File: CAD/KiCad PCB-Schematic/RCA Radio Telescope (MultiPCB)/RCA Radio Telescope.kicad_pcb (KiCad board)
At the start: 2 copper layers, 298.5 x 183.4 mm, 72 parts, among them J1 5V In For Filter Board, J10 FILTER_OUT, J11 ANT, J11 Screw_Terminal_01x04, J13 Screw_Terminal_01x04, J15 ANT, J2 9-12V From PoE Splitter, J3 3V Out For LNA, J4 5V Out For Filter Board, J5 Input from SDR, J7 USB_A, J8 USB_A, J9 ANT, Q1 DMP4047LFDE-7, U13 MAX8510EXK30T, U14 TPS62133RGTR, U15 BPF-A1340+, U3 SKY13588-460LF, U4 SKY13588-460LF, U5 SN74AVC2T45DCUR, U6 MIC5365-1.8YC5-TR, U7 MIC5365-3.3YC5-TR

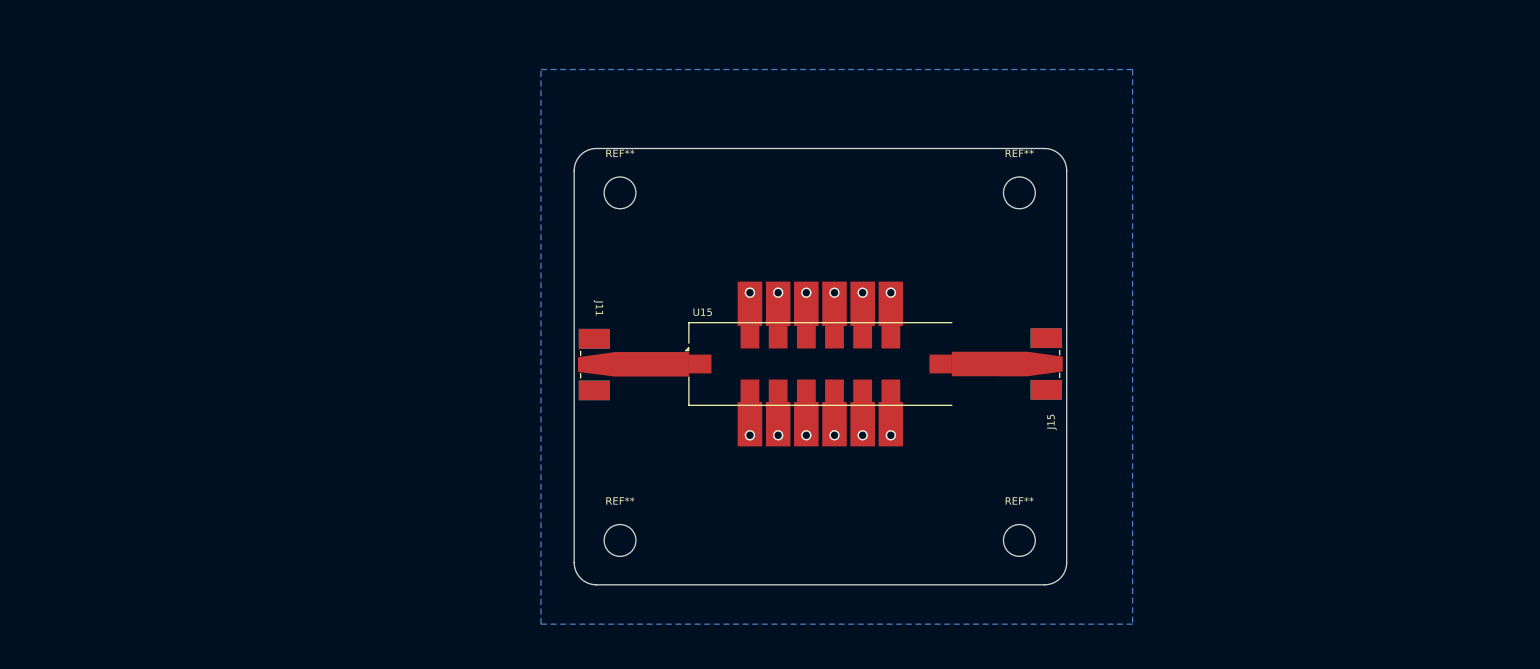
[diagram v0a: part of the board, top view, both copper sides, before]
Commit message: Add 1.6 GHZ Matching Network PCB v1.0
- Same design as original board, but with 1.6 GHz matching network
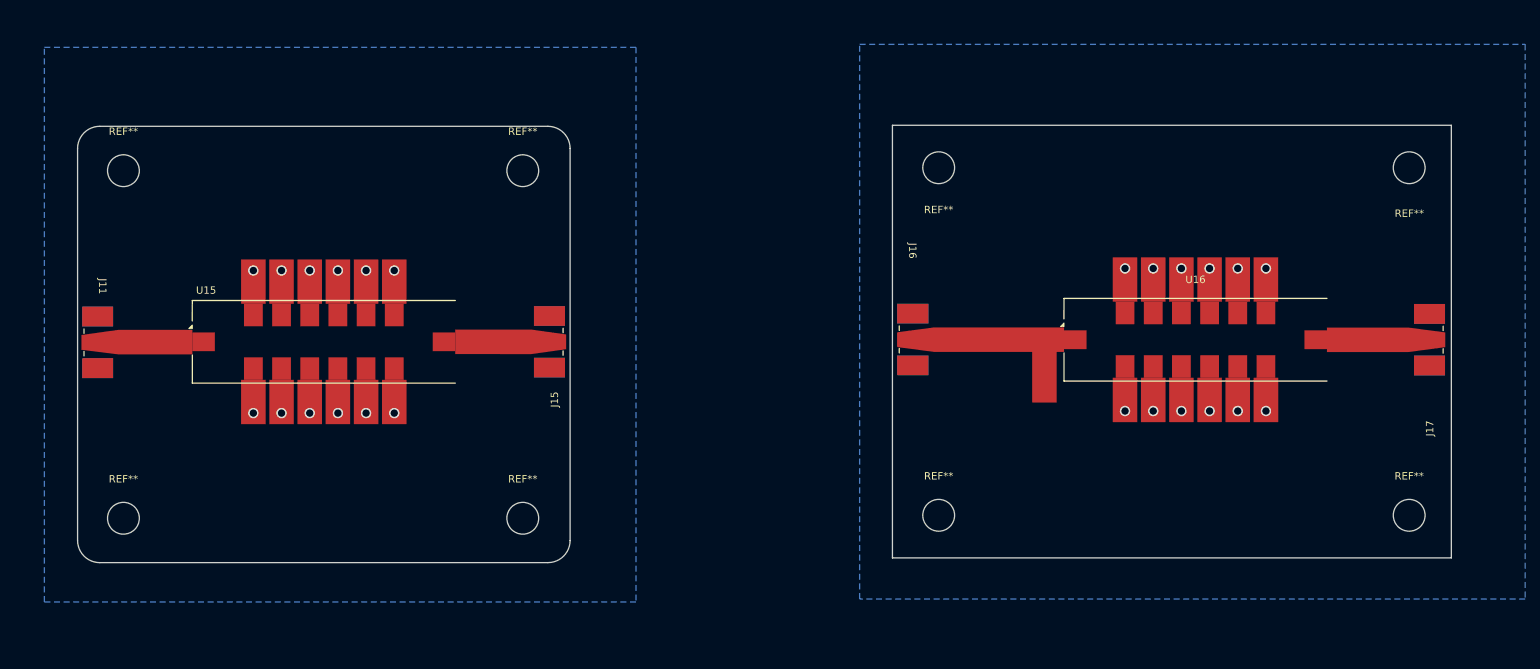
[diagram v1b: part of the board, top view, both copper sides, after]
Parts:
- added J16: ANT, Library:CONN_142-0711-821_CIN, F.Cu at (310.6, 71.8)
- added J17: ANT, Library:CONN_142-0711-821_CIN, F.Cu at (370.5, 71.9)
- added REF**: MountingHole_4.3mm_M4, MountingHole:MountingHole_4.3mm_M4, F.Cu at (372.7, 95.6)
- added REF**: MountingHole_4.3mm_M4, MountingHole:MountingHole_4.3mm_M4, F.Cu at (309.1, 95.6)
- added REF**: MountingHole_4.3mm_M4, MountingHole:MountingHole_4.3mm_M4, F.Cu at (309.1, 48.6)
- added REF**: MountingHole_4.3mm_M4, MountingHole:MountingHole_4.3mm_M4, F.Cu at (372.7, 48.6)
- added SIXSF: Kikit_Board_Label, Library:Kikit_Board_Label, F.Cu at (319.1, 42.6)
- added U16: BPF-A1340+, RF_Mini-Circuits:Mini-Circuits_HQ1157, F.Cu at (343.8, 71.9)
- moved J11 67.2 mm to (200.3, 72.2)
- moved J15 67.2 mm to (251.5, 72.1)
- moved REF** 67.2 mm to (252.8, 96.0)
- moved REF** 67.2 mm to (198.8, 49.0)
- moved REF** 67.2 mm to (198.8, 96.0)
- moved REF** 67.2 mm to (252.8, 49.0)
- moved SF 67.2 mm to (208.8, 43.0)
- moved U15 67.2 mm to (225.9, 72.1)
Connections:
- J11 pad 4: /SMDFilter/GND -> (no net)
- J11 pad 6: /SMDFilter/GND -> (no net)
- J15 pad 4: /SMDFilter/GND -> (no net)
- J15 pad 6: /SMDFilter/GND -> (no net)
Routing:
- net /1-6GHz-SMDFilter/GND: vias 0 -> 12
- added copper zone on B.Cu, net /1-6GHz-SMDFilter/GND
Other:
- board size 298.5 x 183.4 mm -> 350.5 x 183.4 mm
- board text added: "1.6GHz Matching Network SMD Filter PCB Rev v1.0 4/25/2025"

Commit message: Added Coupled Lines Filter PCB v1.0 and Exported PD Board Step File
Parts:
- added J18: ANT, Library:CONN_142-0711-821_CIN, F.Cu at (458.9, 42.5)
- added J19: ANT, Library:CONN_142-0711-821_CIN, F.Cu at (605.7, 48.5)
- added SIXSF: Kikit_Board_Label, Library:Kikit_Board_Label, F.Cu at (467.8, 28.3)
- moved J10 59.5 mm to (89.2, 222.8)
- moved MN 59.5 mm to (98.7, 173.8)
- moved C13 59.5 mm to (131.7, 201.8)
- moved C14 59.5 mm to (131.8, 243.8)
- moved C15 59.5 mm to (131.7, 223.8)
- moved J13 59.5 mm to (112.9, 176.8)
- moved J9 59.5 mm to (183.7, 222.8)
- moved L1 59.5 mm to (142.7, 202.8)
- moved L3 59.5 mm to (142.7, 242.8)
- moved L4 59.5 mm to (142.7, 222.8)
- moved U3 59.5 mm to (156.1, 222.8)
- moved U4 59.5 mm to (116.7, 222.8)
- moved J11 13.0 mm to (212.8, 68.7)
- moved J15 13.0 mm to (264.0, 68.7)
- moved J16 13.0 mm to (323.1, 68.3)
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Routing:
- added copper zone on B.Cu, net /Coupled Lines Filter/GND
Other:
- board size 350.5 x 183.4 mm -> 585.8 x 231 mm
- board text added: "Coupled Lines SMD Filter PCB Rev v1.0 4/25/2025"

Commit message: RF Boards Redo (WIP)
- Overhauling current RF boards to keep 4 RF boards in total
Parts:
- removed C13, C14, C15: C, Capacitor_SMD:C_0805_2012Metric
- removed J13: Screw_Terminal_01x04, Connector_PinHeader_2.54mm:PinHeader_1x04_P2.54mm_Vertical
- removed L1, L3, L4: L, Inductor_SMD:L_0805_2012Metric
- removed MN, SIXSF (x2): Kikit_Board_Label, Library:Kikit_Board_Label
- removed the REF** at (385.2, 92.1)
- removed the REF** at (321.6, 92.1)
- removed the REF** at (321.6, 45.1)
- removed the REF** at (385.2, 45.1)
- added C1: 1 uF, Capacitor_SMD:C_0805_2012Metric, F.Cu at (97.0, 183.0)
- added C2: 1 uF, Capacitor_SMD:C_0805_2012Metric, F.Cu at (101.0, 183.1)
- added C3: 1 uF, Capacitor_SMD:C_0805_2012Metric, F.Cu at (108.0, 183.1)
- added C4: 1 uF, Capacitor_SMD:C_0805_2012Metric, F.Cu at (111.0, 183.1)
- added J1: Screw_Terminal_01x04, Library:PHOENIX_1729144, F.Cu at (75.1, 184.6)
- added J11: ANT, Library:CONN_142-0711-821_CIN, F.Cu at (162.5, 118.5)
- added J15: ANT, Library:CONN_142-0711-821_CIN, F.Cu at (162.5, 128.6)
- added TP12: FCTRL_VIN, Library:TestPoint_Pad_D1.0mm_Edit, F.Cu at (108.0, 205.0)
- added TP13: FCTRL_1V8, Library:TestPoint_Pad_D1.0mm_Edit, F.Cu at (108.0, 208.1)
- added TP14: FCTRL_3V3, Library:TestPoint_Pad_D1.0mm_Edit, F.Cu at (108.0, 211.1)
- added TP15: FCTRL_GND, Library:TestPoint_Pad_1.5x1.5mm_Edit, F.Cu at (69.9, 226.5)
- added U5: SN74AVC2T45DCUR, Library:DCU8, F.Cu at (99.0, 177.0)
- added U6: MIC5365-1.8YC5-TR, Library:SOT65P210X110-5N, F.Cu at (92.0, 183.0)
- added U7: MIC5365-3.3YC5-TR, Library:SOT65P210X110-5N, F.Cu at (82.0, 216.0)
- moved J19 449.6 mm to (273.7, 351.7)
- moved J16 426.3 mm to (8.38, 356.0)
- moved J18 418.0 mm to (177.6, 351.7)
- moved J17 399.7 mm to (104.4, 355.0)
- moved U16 397.2 mm to (81.7, 355.4)
- moved J9 153.5 mm to (31.0, 206.8), turned to 0 degrees
- moved U3 94.6 mm to (61.7, 227.0), turned to 0 degrees
- moved U4 51.0 mm to (66.0, 227.0), turned to 0 degrees
- moved J10 28.3 mm to (68.0, 204.0), turned to 0 degrees
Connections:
- net /1-6GHz-SMDFilter/GND renamed /Matched SMD Filter/GND
- net /1-6GHz-SMDFilter/SIGNAL_IN renamed /Matched SMD Filter/SIGNAL_IN
- net /1-6GHz-SMDFilter/SIGNAL_OUT renamed /Matched SMD Filter/SIGNAL_OUT
- net /MatchNetwork/+3V3 renamed /RFSwitchFilter/+3V3
- net /MatchNetwork/ANT renamed /RFSwitchFilter/ANT
- net /MatchNetwork/FILTER_OUT renamed /RFSwitchFilter/FILTER_OUT
- net /MatchNetwork/INT_CTRL_V1 renamed /RFSwitchFilter/INT_CTRL_V1
- net /MatchNetwork/INT_CTRL_V2 renamed /RFSwitchFilter/INT_CTRL_V2
- J18 pad 1: /Coupled Lines Filter/SIGNAL_IN -> /Matched Distributive Filter/SIGNAL_IN
- J18 pad 4: /Coupled Lines Filter/GND -> (no net)
- J18 pad 6: /Coupled Lines Filter/GND -> (no net)
- J19 pad 1: /Coupled Lines Filter/SIGNAL_OUT -> /Matched Distributive Filter/SIGNAL_IN
- U3 pad 1: /MatchNetwork/FILTERA_IN -> /RFSwitchFilter/FILTERA_IN
- U3 pad 3: /MatchNetwork/FILTERC_IN -> /RFSwitchFilter/FILTERC_IN
- U3 pad 9: /MatchNetwork/FILTERB_IN -> /RFSwitchFilter/FILTERB_IN
- U4 pad 1: /MatchNetwork/FILTERB_OUT -> /RFSwitchFilter/FILTERB_IN
- U4 pad 3: /MatchNetwork/FILTERC_OUT -> /RFSwitchFilter/FILTERC_IN
- U4 pad 9: /MatchNetwork/FILTERA_OUT -> /RFSwitchFilter/FILTERA_IN
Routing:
- net /RFSwitchFilter/INT_CTRL_V2: track 152.7 -> 0.00 mm, vias 2 -> 0
- net /RFSwitchFilter/+3V3: track 150.0 -> 0.00 mm, vias 3 -> 0
- net /RFSwitchFilter/INT_CTRL_V1: track 144.7 -> 0.00 mm, vias 3 -> 0
- net /MatchNetwork/FILTERA_OUT: track 39.0 -> 0.00 mm
- net /MatchNetwork/FILTERB_OUT: track 37.8 -> 0.00 mm
- net /MatchNetwork/FILTERC_OUT: track 27.5 -> 0.00 mm
- net /MatchNetwork/FILTERA_IN: track 26.2 -> 0.00 mm
- net /MatchNetwork/FILTERB_IN: track 25.0 -> 0.00 mm
- net /RFSwitchFilter/FILTER_OUT: track 19.2 -> 0.00 mm
- net /RFSwitchFilter/ANT: track 19.2 -> 0.00 mm
- net /MatchNetwork/FILTERC_IN: track 14.3 -> 0.00 mm
- net (no net): track 0.00 -> 5.24 mm
- net /Matched SMD Filter/GND: vias 12 -> 0
- net /MN_GND: vias 156 -> 0
- removed copper zone on B.Cu, net /Coupled Lines Filter/GND
- removed copper zone on B.Cu, net /MN_GND
- removed copper zone on F.Cu, net /MN_GND
- removed copper zone on B.Cu, net /Matched SMD Filter/GND
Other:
- board size 585.8 x 231 mm -> 243.8 x 78.8 mm
- board text added: "Matched Distributive Filter PCB Rev v1.3 4/11/2025"
- board text added: "Matched SMD Filter PCB Rev v1.0 4/29/2025"
- board text removed: "1.6GHz Matching Network SMD Filter PCB Rev v1.0 4/25/2025"
- board text removed: "Coupled Lines SMD Filter PCB Rev v1.0 4/25/2025"
- board text removed: "Matching Network PCB Rev v1.0 4/3/2025"

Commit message: Added 4 RF Board Designs into KiCAD project
- Added Matched SMD Filter Board, Matched Distributive Filter Board, RF Switch Filter Board, and kept original SMD Filter Board
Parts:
- removed the C1 at (151.0, 33.0)
- removed the C2 at (151.0, 38.5)
- removed the C3 at (143.1, 33.9)
- removed the C4 at (145.2, 37.4)
- removed FC: Kikit_Board_Label, Library:Kikit_Board_Label
- removed the J1 at (156.6, 34.5)
- removed the J11 at (162.5, 118.5)
- removed the J11 at (141.0, 41.0)
- removed the J15 at (162.5, 128.6)
- removed the REF** at (265.3, 92.5)
- removed the REF** at (211.3, 45.5)
- removed the REF** at (211.3, 92.5)
- removed the REF** at (265.3, 45.5)
- removed the TP12 at (153.6, 29.2)
- removed the TP13 at (145.1, 34.5)
- removed the TP14 at (143.1, 36.7)
- removed TP15 (x2): FCTRL_GND, Library:TestPoint_Pad_1.5x1.5mm_Edit
- removed the U5 at (140.6, 34.6)
- removed the U6 at (148.1, 33.2)
- removed the U7 at (148.0, 37.6)
- added MDF: Kikit_Board_Label, Library:Kikit_Board_Label, F.Cu at (40.9, 222.2)
- added MSF: Kikit_Board_Label, Library:Kikit_Board_Label, F.Cu at (40.5, 136.1)
- added REF**: MountingHole_4.3mm_M4, MountingHole:MountingHole_4.3mm_M4, F.Cu at (135.0, 256.0)
- added REF**: MountingHole_4.3mm_M4, MountingHole:MountingHole_4.3mm_M4, F.Cu at (186.0, 65.0)
- added REF**: MountingHole_4.3mm_M4, MountingHole:MountingHole_4.3mm_M4, F.Cu at (186.0, 110.0)
- added REF**: MountingHole_4.3mm_M4, MountingHole:MountingHole_4.3mm_M4, F.Cu at (35.0, 256.0)
- added REF**: MountingHole_4.3mm_M4, MountingHole:MountingHole_4.3mm_M4, F.Cu at (36.0, 142.0)
- added REF**: MountingHole_4.3mm_M4, MountingHole:MountingHole_4.3mm_M4, F.Cu at (257.0, 175.0)
- added REF**: MountingHole_4.3mm_M4, MountingHole:MountingHole_4.3mm_M4, F.Cu at (143.0, 142.0)
- added REF**: MountingHole_4.3mm_M4, MountingHole:MountingHole_4.3mm_M4, F.Cu at (307.0, 110.0)
- added REF**: MountingHole_4.3mm_M4, MountingHole:MountingHole_4.3mm_M4, F.Cu at (307.0, 65.0)
- added REF**: MountingHole_4.3mm_M4, MountingHole:MountingHole_4.3mm_M4, F.Cu at (36.0, 171.0)
- added REF**: MountingHole_4.3mm_M4, MountingHole:MountingHole_4.3mm_M4, F.Cu at (135.0, 229.0)
- added REF**: MountingHole_4.3mm_M4, MountingHole:MountingHole_4.3mm_M4, F.Cu at (202.0, 175.0)
- added REF**: MountingHole_4.3mm_M4, MountingHole:MountingHole_4.3mm_M4, F.Cu at (202.0, 222.0)
- added REF**: MountingHole_4.3mm_M4, MountingHole:MountingHole_4.3mm_M4, F.Cu at (143.0, 171.0)
- added REF**: MountingHole_4.3mm_M4, MountingHole:MountingHole_4.3mm_M4, F.Cu at (35.0, 229.0)
- added REF**: MountingHole_4.3mm_M4, MountingHole:MountingHole_4.3mm_M4, F.Cu at (257.0, 222.0)
- added RFS: Kikit_Board_Label, Library:Kikit_Board_Label, F.Cu at (194.3, 59.0)
- added U17: BPF-A355, RF_Mini-Circuits:Mini-Circuits_HQ1157, F.Cu at (279.0, 95.9)
- C1, C2, C3, C4, TP12, TP13, TP14, U6, U7: moved to B.Cu
- J5: value Input from SDR -> 5V From SDR; footprint Library:PHOENIX_1729144 -> Library:CONN_1729128_PXC
- U5: value SN74AVC2T45DCUR -> SN74AVC2T244DQER; footprint Library:DCU8 -> Library:SON35P140X100X40-8N; moved to B.Cu
- moved J10 260.4 mm to (304.8, 95.8), turned to 90 degrees
- moved U4 231.8 mm to (257.1, 95.9), turned to -90 degrees
- moved U7 213.7 mm to (242.0, 74.4), turned to -90 degrees
- moved U16 202.4 mm to (114.6, 155.6)
- moved J17 202.4 mm to (140.6, 155.9)
- moved J16 202.2 mm to (38.1, 156.0)
- moved J1 197.5 mm to (228.3, 60.0), turned to 180 degrees
- moved TP12 191.0 mm to (244.5, 71.4), turned to 180 degrees
- moved J9 190.9 mm to (187.4, 97.4), turned to -90 degrees
- moved U3 190.3 mm to (201.1, 97.4), turned to 90 degrees
- moved TP14 188.6 mm to (239.0, 75.4), turned to 180 degrees
- moved TP13 180.9 mm to (231.0, 75.4), turned to 180 degrees
- moved U6 178.6 mm to (233.7, 74.4), turned to -90 degrees
- moved J18 178.3 mm to (36.8, 242.3)
- moved J19 178.1 mm to (133.1, 242.3)
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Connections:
- C1 pad 2: /MN_GND -> /RFS_GND
- C2 pad 2: /MN_GND -> /RFS_GND
- C3 pad 1: /MN_GND -> /RFS_GND
- C4 pad 1: /MN_GND -> /RFS_GND
- J1 pad 1: /MN_GND -> /RFS_GND
- J18 pad 1: /Matched Distributive Filter/SIGNAL_IN -> /Matched Distributive Filter/GND
- J19 pad 1: /Matched Distributive Filter/SIGNAL_IN -> /Matched Distributive Filter/GND
- J5 pad 1: /SDR_GPO_VDD -> /RFSwitchFilter/5V_IN
- J5 pad 2: /SDR_GPO_0 -> /RFS_GND
- U3 pad 10: /MN_GND -> /RFS_GND
- U3 pad 12: /MN_GND -> /RFS_GND
- U3 pad 13: /MN_GND -> /RFS_GND
- U3 pad 2: /MN_GND -> /RFS_GND
- U3 pad 7: /MN_GND -> /RFS_GND
- U3 pad 8: /MN_GND -> /RFS_GND
- U4 pad 10: /MN_GND -> /RFS_GND
- U4 pad 11: /RFSwitchFilter/FILTER_OUT -> Net-(U17-IN)
- U4 pad 12: /MN_GND -> /RFS_GND
- U4 pad 13: /MN_GND -> /RFS_GND
- U4 pad 2: /MN_GND -> /RFS_GND
- U4 pad 7: /MN_GND -> /RFS_GND
- U4 pad 8: /MN_GND -> /RFS_GND
- U5 pad 4: /MN_GND -> /RFSwitchFilter/VDD_REF
- U5 pad 5: /RFSwitchFilter/VDD_REF -> /RFS_GND
- U6 pad 2: /MN_GND -> /RFS_GND
- U7 pad 2: /MN_GND -> /RFS_GND
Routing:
- net /RFSwitchFilter/INT_CTRL_V1: track 0.00 -> 120.4 mm, vias 0 -> 4
- net /RFSwitchFilter/INT_CTRL_V2: track 0.00 -> 115.8 mm, vias 0 -> 4
- net /RFSwitchFilter/+3V3: track 0.00 -> 102.6 mm, vias 0 -> 2
- net /RFS_GND: track 0.00 -> 71.7 mm, vias 0 -> 16
- net /RFSwitchFilter/+1V8: track 0.00 -> 41.0 mm
- net /RFSwitchFilter/5V_IN: track 0.00 -> 26.4 mm
- net /FiltersCTRL/5V_IN: track 25.2 -> 0.00 mm
- net /RFSwitchFilter/VDD_REF: track 0.00 -> 20.0 mm, vias 0 -> 1
- net /RFSwitchFilter/CNTR_V2: track 0.00 -> 19.3 mm
- net /SDR_GPO_VDD: track 15.3 -> 0.00 mm
- net /RFSwitchFilter/CNTR_V1: track 0.00 -> 13.0 mm
- net /FiltersCTRL/+3V3: track 10.3 -> 0.00 mm
- net /SDR_GPO_0: track 8.58 -> 0.00 mm
- net /SDR_GPO_1: track 7.92 -> 0.00 mm
- net /FiltersCTRL/VSEL_1: track 7.49 -> 0.00 mm
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- added copper zone on B.Cu, net /Matched Distributive Filter/GND
- added copper zone on B.Cu, net /Matched SMD Filter/GND
- added copper zone on B.Cu, net /RFS_GND
- removed copper zone on B.Cu, net /FILTERCTRL_GND
- removed copper zone on F.Cu, net /FILTERCTRL_GND
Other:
- board size 243.8 x 78.8 mm -> 284.8 x 238.1 mm
- board text added: "Matched Distributive Filter PCB Rev v1.0 4/29/2025"
- board text added: "RF Switch Filter PCB Rev v1.0 4/29/2025"
- board text removed: "5V IN"
- board text removed: "Filter Control PCB Rev v1.1 4/4/2025"
- board text removed: "GPO0"
- board text removed: "GPO1"
- board text removed: "Matched Distributive Filter PCB Rev v1.3 4/11/2025"
- board text removed: "PSU ECE Capstone Team 11 RCA Radio Telescope Filter Control Board v1.0 (3/30/2025)"
- board text removed: "SDR GPO IN"
- board text removed: "VDD"

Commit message: Updated PCB size for RF boards, and relocated power circuitry for RF switch board
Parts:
- moved J15 115.9 mm to (366.1, 164.3)
- moved REF** 115.6 mm to (367.6, 141.5)
- moved REF** 115.6 mm to (312.6, 141.5)
- moved REF** 115.6 mm to (312.6, 188.5)
- moved REF** 115.6 mm to (367.6, 188.5)
- moved SF 115.6 mm to (323.1, 135.2)
- moved U15 115.6 mm to (340.2, 164.4)
- moved J11 115.3 mm to (314.3, 164.4)
- moved REF** 90.0 mm to (113.0, 184.0)
- moved REF** 90.0 mm to (213.0, 184.0)
- moved MDF 87.2 mm to (115.0, 176.2)
- moved J19 82.2 mm to (211.1, 216.3)
- moved J18 82.2 mm to (114.8, 216.3)
- moved REF** 78.3 mm to (113.0, 249.0)
- moved REF** 78.3 mm to (213.0, 249.0)
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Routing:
- net /RFS_GND: track 71.7 -> 76.8 mm
- net /RFSwitchFilter/+1V8: track 41.0 -> 38.3 mm
- net /RFSwitchFilter/5V_IN: track 26.4 -> 27.2 mm
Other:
- board size 284.8 x 238.1 mm -> 345.9 x 232.2 mm
- board text added: "Matched Distributive Filter PCB Rev v1.1 4/30/2025"
- board text added: "Matched SMD Filter PCB Rev v1.1 4/30/2025"
- board text added: "RF Switch Filter PCB Rev v1.1 4/30/2025"
- board text removed: "Matched Distributive Filter PCB Rev v1.0 4/29/2025"
- board text removed: "Matched SMD Filter PCB Rev v1.0 4/29/2025"
- board text removed: "RF Switch Filter PCB Rev v1.0 4/29/2025"

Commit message: Update RF Board Designs
- Added Vias to SMA connector pads
- Removed wiring for control/power wires for RF switches
- Adjusted grounding for RF filters
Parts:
- moved J16 0.39 mm to (40.5, 118.6)
- moved REF** 0.29 mm to (314.0, 33.0)
- moved REF** 0.29 mm to (193.0, 33.0)
- moved J17 0.11 mm to (142.7, 118.6)
- moved REF** 0.07 mm to (314.0, 97.0)
- moved REF** 0.07 mm to (193.0, 97.0)
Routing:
- net /RFSwitchFilter/INT_CTRL_V1: track 120.4 -> 32.6 mm
- net /RFSwitchFilter/INT_CTRL_V2: track 115.8 -> 29.5 mm
- net /RFSwitchFilter/+3V3: track 103.0 -> 22.9 mm, vias 2 -> 4
- net /RFS_GND: track 76.8 -> 77.8 mm
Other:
- outline, holes or cut-outs redrawn
- board text added: "Matched Distributive Filter PCB Rev v1.2 5/2/2025"
- board text added: "Matched SMD Filter PCB Rev v1.2 5/2/2025"
- board text added: "RF Switch Filter PCB Rev v1.2 5/2/2025"
- board text added: "SMD Filter PCB Rev v1.4 5/2/2025"
- board text removed: "Matched Distributive Filter PCB Rev v1.1 4/30/2025"
- board text removed: "Matched SMD Filter PCB Rev v1.1 4/30/2025"
- board text removed: "RF Switch Filter PCB Rev v1.1 4/30/2025"
- board text removed: "SMD Filter PCB Rev v1.3 4/11/2025"

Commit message: Updated RF Board Hole Data and Exported STEPs for 3D Modeling
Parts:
- removed the REF** at (213.0, 249.0)
- removed the REF** at (113.0, 249.0)
- removed the REF** at (213.0, 184.0)
- removed the REF** at (113.0, 184.0)
- added REF**: MountingHole_4.3mm_M4, MountingHole:MountingHole_4.3mm_M4, F.Cu at (70.3, 359.5)
- added REF**: MountingHole_4.3mm_M4, MountingHole:MountingHole_4.3mm_M4, F.Cu at (169.3, 291.5)
- added REF**: MountingHole_4.3mm_M4, MountingHole:MountingHole_4.3mm_M4, F.Cu at (169.3, 359.5)
- added REF**: MountingHole_4.3mm_M4, MountingHole:MountingHole_4.3mm_M4, F.Cu at (70.3, 291.5)
- moved SF 173.3 mm to (267.8, 299.4)
- moved J11 173.3 mm to (259.0, 328.6)
- moved J15 173.3 mm to (310.8, 328.5)
- moved REF** 173.3 mm to (312.3, 352.7)
- moved REF** 173.3 mm to (312.3, 305.7)
- moved REF** 173.3 mm to (257.3, 305.7)
- moved REF** 173.3 mm to (257.3, 352.7)
- moved U15 173.3 mm to (284.9, 328.6)
- moved REF** 127.0 mm to (236.2, 216.4)
- moved REF** 127.0 mm to (357.2, 216.4)
- moved C1 126.1 mm to (290.8, 151.1)
- moved C2 126.1 mm to (293.3, 151.1)
- moved C4 126.1 mm to (296.6, 156.6)
- moved J1 126.1 mm to (278.5, 146.1)
- moved J10 126.1 mm to (355.1, 181.9)
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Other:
- board size 345.9 x 232.2 mm -> 335 x 340.9 mm
- board text added: "Hole Info Length: 105 mm Width: 54 mm Hole Size: M4"
- board text added: "Hole Info Length: 121 mm Width: 65 mm Hole Size: M4"
- board text added: "Hole Info Length: 55 mm Width: 47 mm Hole Size: M4"
- board text added: "Hole Info: Length: 99 mm Width: 68 mm Hole Size: M4"
- board text added: "Matched Distributive Filter PCB Rev v1.3 5/2/2025"
- board text added: "Matched SMD Filter PCB Rev v1.3 5/2/2025"
- board text added: "Note: Standoffs for RF Switch Filter should be a bit higher to accommodate coax underneath"
- board text added: "RF Switch Filter PCB Rev v1.3 5/2/2025"
- board text removed: "Length: 54 mm Width: 47 mm Hole Diameter: 4 mm"
- board text removed: "Matched Distributive Filter PCB Rev v1.2 5/2/2025"
- board text removed: "Matched SMD Filter PCB Rev v1.2 5/2/2025"
- board text removed: "RF Switch Filter PCB Rev v1.2 5/2/2025"
